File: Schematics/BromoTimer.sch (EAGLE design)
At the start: 29 parts, among them IC1 PIC16F687, IC2 7805TV, K1 G2R2A, K2 G2R2A, Q1 BC548B, Q2 BC548B, Q3 BC548B, X1 AC_IN, X4 22-23-2031, X5 AC_OUT

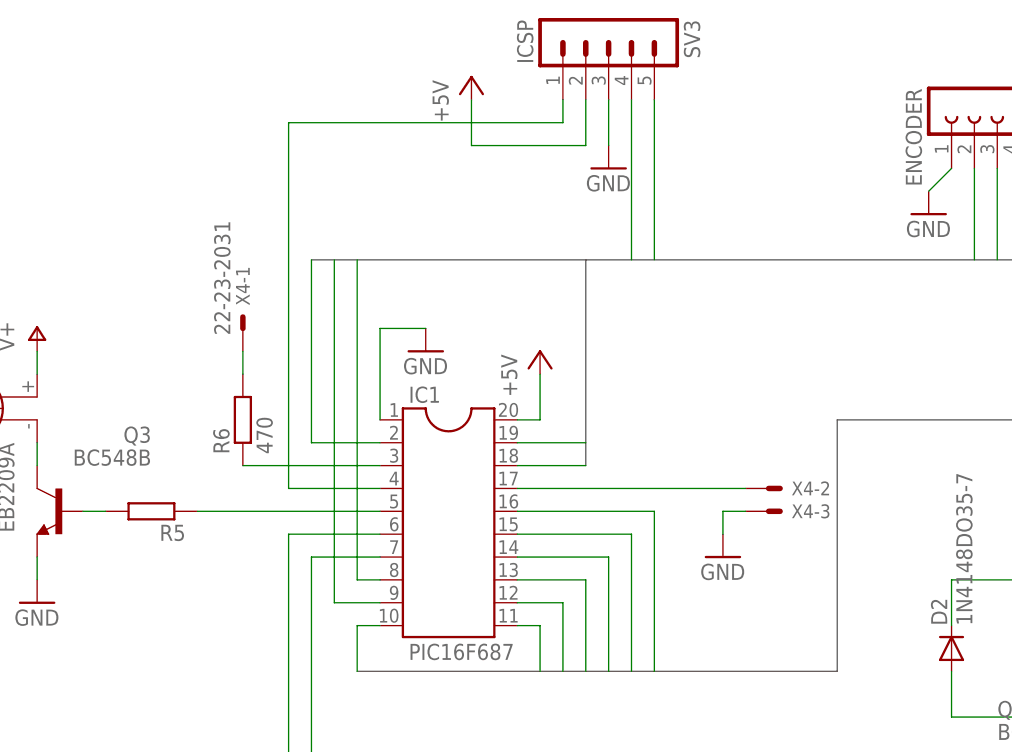
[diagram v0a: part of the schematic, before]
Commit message: Add support for lid state sensor
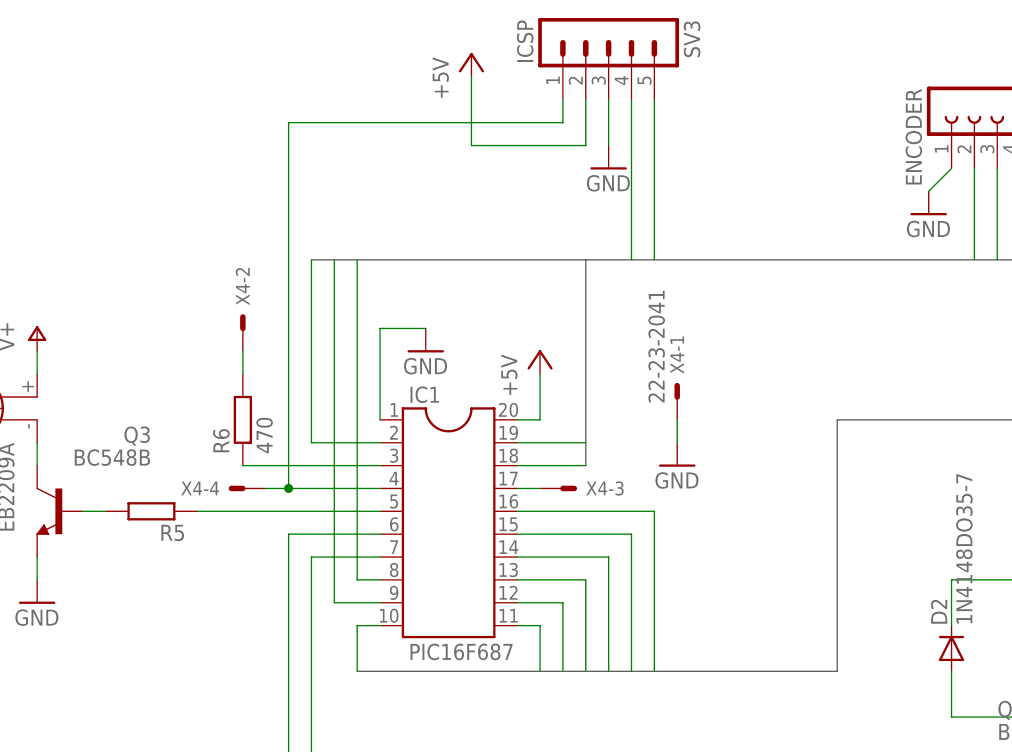
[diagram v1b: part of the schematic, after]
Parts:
- X4: value 22-23-2031 -> 22-23-2041; device con-molex:22-23-2031 -> con-molex:22-23-2041
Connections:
- net GND: now also X4-1.S; no longer X4-3.S
- net N$13: now also X4-3.S; no longer X4-2.S
- net N$15: now also X4-4.S
- net N$21: now also X4-2.S; no longer X4-1.S
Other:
- moved on the sheet: X4-1, X4-2, X4-3
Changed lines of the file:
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@@
 <?xml version="1.0" encoding="utf-8"?>
 <!DOCTYPE eagle SYSTEM "eagle.dtd">
-<eagle version="6.3">
+<eagle version="6.4">
 <drawing>
 <settings>
@@
 <part name="GND11" library="supply1" deviceset="GND" device=""/>
 <part name="P+10" library="supply1" deviceset="V+" device=""/>
-<part name="X4" library="con-molex" deviceset="22-23-2031" device=""/>
+<part name="X4" library="con-molex" deviceset="22-23-2041" device=""/>
 <part name="GND9" library="supply1" deviceset="GND" device=""/>
 <part name="SG1" library="buzzer" deviceset="EB2209A" device=""/>
@@
 <instance part="D2" gate="G$1" x="170.18" y="101.6" rot="R90"/>
 <instance part="SV3" gate="G$1" x="132.08" y="170.18" rot="R270"/>
-<instance part="P+9" gate="1" x="116.84" y="165.1"/>
+<instance part="P+9" gate="1" x="116.84" y="167.64"/>
 <instance part="GND10" gate="1" x="132.08" y="154.94"/>
 <instance part="D3" gate="1" x="40.64" y="71.12" rot="R180"/>
@@
 <instance part="GND11" gate="1" x="68.58" y="106.68"/>
 <instance part="P+10" gate="1" x="68.58" y="137.16"/>
-<instance part="X4" gate="-1" x="91.44" y="137.16" rot="R90"/>
-<instance part="X4" gate="-2" x="149.86" y="119.38"/>
-<instance part="X4" gate="-3" x="149.86" y="116.84"/>
-<instance part="GND9" gate="1" x="144.78" y="111.76"/>
+<instance part="X4" gate="-1" x="139.7" y="129.54" rot="R90"/>
+<instance part="X4" gate="-2" x="91.44" y="137.16" rot="R90"/>
+<instance part="X4" gate="-3" x="127" y="119.38"/>
+<instance part="GND9" gate="1" x="139.7" y="121.92"/>
 <instance part="SG1" gate="G$1" x="66.04" y="129.54" rot="MR270"/>
 <instance part="TR1" gate="1" x="45.72" y="25.4"/>
@@
 <instance part="X5" gate="-5" x="220.98" y="43.18"/>
 <instance part="F1" gate="1" x="27.94" y="27.94"/>
+<instance part="X4" gate="-4" x="91.44" y="119.38" rot="R180"/>
 </instances>
 <busses>
@@
 <wire x1="129.54" y1="162.56" x2="129.54" y2="157.48" width="0.1524" layer="91"/>
 <wire x1="129.54" y1="157.48" x2="116.84" y2="157.48" width="0.1524" layer="91"/>
-<wire x1="116.84" y1="157.48" x2="116.84" y2="162.56" width="0.1524" layer="91"/>
+<wire x1="116.84" y1="157.48" x2="116.84" y2="165.1" width="0.1524" layer="91"/>
 <pinref part="P+9" gate="1" pin="+5V"/>
 </segment>
@@
 </segment>
 <segment>
-<pinref part="X4" gate="-3" pin="S"/>
-<pinref part="GND9" gate="1" pin="GND"/>
-<wire x1="147.32" y1="116.84" x2="144.78" y2="116.84" width="0.1524" layer="91"/>
-<wire x1="144.78" y1="116.84" x2="144.78" y2="114.3" width="0.1524" layer="91"/>
-</segment>
-<segment>
 <pinref part="Q3" gate="G$1" pin="E"/>
 <pinref part="GND11" gate="1" pin="GND"/>
 <wire x1="68.58" y1="111.76" x2="68.58" y2="109.22" width="0.1524" layer="91"/>
+</segment>
+<segment>
+<pinref part="GND9" gate="1" pin="GND"/>
+<pinref part="X4" gate="-1" pin="S"/>
+<wire x1="139.7" y1="124.46" x2="139.7" y2="127" width="0.1524" layer="91"/>
 </segment>
 </net>
@@
 <wire x1="96.52" y1="160.02" x2="96.52" y2="119.38" width="0.1524" layer="91"/>
 <wire x1="96.52" y1="119.38" x2="106.68" y2="119.38" width="0.1524" layer="91"/>
+<pinref part="X4" gate="-4" pin="S"/>
+<wire x1="93.98" y1="119.38" x2="96.52" y2="119.38" width="0.1524" layer="91"/>
+<junction x="96.52" y="119.38"/>
 </segment>
 </net>
@@
 </segment>
 </net>
-<net name="N$13" class="0">
-<segment>
-<pinref part="IC1" gate="G$1" pin="17"/>
-<pinref part="X4" gate="-2" pin="S"/>
-<wire x1="121.92" y1="119.38" x2="147.32" y2="119.38" width="0.1524" layer="91"/>
-</segment>
-</net>
 <net name="N$18" class="0">
 <segment>
@@
 </segment>
 </net>
-<net name="N$21" class="0">
-<segment>
-<pinref part="X4" gate="-1" pin="S"/>
-<pinref part="R6" gate="G$1" pin="2"/>
-<wire x1="91.44" y1="134.62" x2="91.44" y2="132.08" width="0.1524" layer="91"/>
-</segment>
-</net>
 <net name="N$2" class="0">
 <segment>
@@
 </segment>
 </net>
+<net name="N$13" class="0">
+<segment>
+<pinref part="IC1" gate="G$1" pin="17"/>
+<pinref part="X4" gate="-3" pin="S"/>
+<wire x1="124.46" y1="119.38" x2="121.92" y2="119.38" width="0.1524" layer="91"/>
+</segment>
+</net>
+<net name="N$21" class="0">
+<segment>
+<pinref part="X4" gate="-2" pin="S"/>
+<pinref part="R6" gate="G$1" pin="2"/>
+<wire x1="91.44" y1="134.62" x2="91.44" y2="132.08" width="0.1524" layer="91"/>
+</segment>
+</net>

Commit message: Clean up R1
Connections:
- net +5V: now also R1.S; no longer R1.A
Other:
- moved on the sheet: R1
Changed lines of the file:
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@@
 <instance part="P+2" gate="1" x="124.46" y="134.62"/>
 <instance part="GND3" gate="1" x="193.04" y="142.24"/>
-<instance part="GND4" gate="1" x="228.6" y="139.7"/>
+<instance part="GND4" gate="1" x="223.52" y="149.86"/>
 <instance part="P+3" gate="1" x="198.12" y="170.18"/>
-<instance part="R1" gate="G$1" x="220.98" y="147.32"/>
+<instance part="R1" gate="G$1" x="220.98" y="137.16"/>
 <instance part="R2" gate="G$1" x="200.66" y="147.32" rot="R180"/>
-<instance part="P+4" gate="1" x="215.9" y="142.24"/>
+<instance part="P+4" gate="1" x="228.6" y="144.78"/>
 <instance part="Q1" gate="G$1" x="185.42" y="86.36"/>
 <instance part="Q2" gate="G$1" x="185.42" y="43.18"/>
@@
 </segment>
 <segment>
-<pinref part="P+4" gate="1" pin="+5V"/>
-<wire x1="215.9" y1="139.7" x2="215.9" y2="137.16" width="0.1524" layer="91"/>
-<pinref part="R1" gate="G$1" pin="A"/>
-<wire x1="215.9" y1="137.16" x2="220.98" y2="137.16" width="0.1524" layer="91"/>
-<wire x1="220.98" y1="137.16" x2="220.98" y2="142.24" width="0.1524" layer="91"/>
-</segment>
-<segment>
 <pinref part="SV3" gate="G$1" pin="2"/>
 <wire x1="129.54" y1="162.56" x2="129.54" y2="157.48" width="0.1524" layer="91"/>
@@
 <junction x="187.96" y="109.22"/>
 </segment>
+<segment>
+<pinref part="P+4" gate="1" pin="+5V"/>
+<wire x1="228.6" y1="142.24" x2="228.6" y2="137.16" width="0.1524" layer="91"/>
+<pinref part="R1" gate="G$1" pin="S"/>
+<wire x1="228.6" y1="137.16" x2="226.06" y2="137.16" width="0.1524" layer="91"/>
+</segment>
 </net>
 <net name="GND" class="0">
@@
 <pinref part="GND4" gate="1" pin="GND"/>
 <pinref part="SV2" gate="G$1" pin="12"/>
-<wire x1="228.6" y1="142.24" x2="228.6" y2="152.4" width="0.1524" layer="91"/>
-<wire x1="228.6" y1="152.4" x2="223.52" y2="152.4" width="0.1524" layer="91"/>
 <wire x1="223.52" y1="152.4" x2="223.52" y2="154.94" width="0.1524" layer="91"/>
 </segment>
@@
 <segment>
 <pinref part="SV2" gate="G$1" pin="11"/>
-<wire x1="220.98" y1="154.94" x2="220.98" y2="152.4" width="0.1524" layer="91"/>
+<wire x1="220.98" y1="154.94" x2="220.98" y2="142.24" width="0.1524" layer="91"/>
 <pinref part="R1" gate="G$1" pin="E"/>
 </segment>

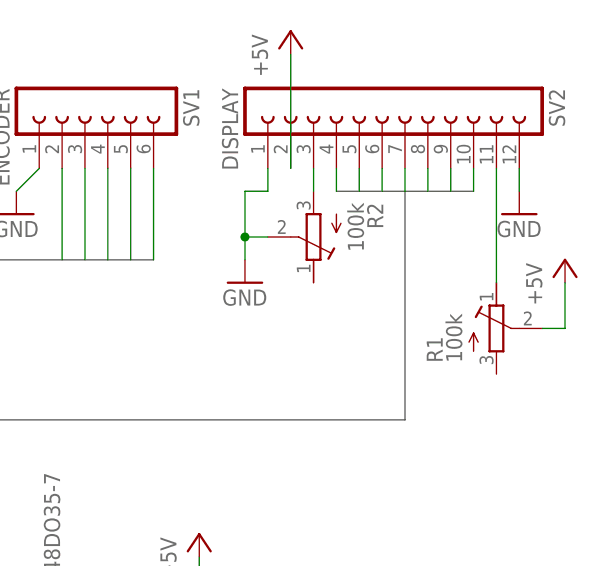
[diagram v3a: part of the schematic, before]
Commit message: Correct trimmer footprints
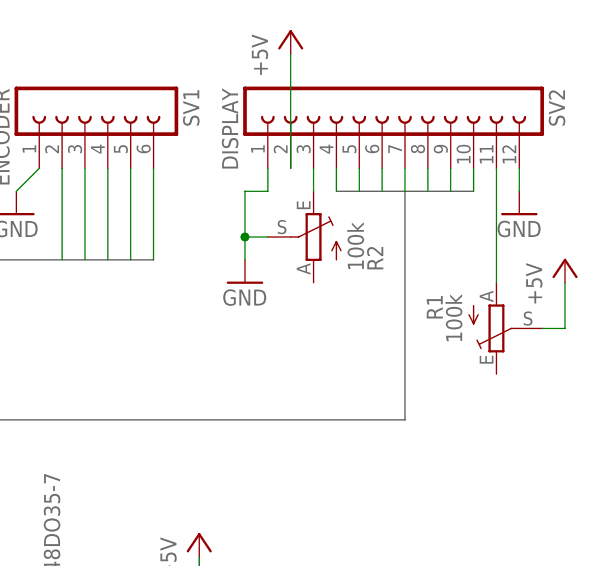
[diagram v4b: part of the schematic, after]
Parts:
- R1, R2: device rcl:R-TRIMMT93YB -> pot:TRIM_EU-CA14H
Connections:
- net N$1: now also R1.A; no longer R1.E
- net N$3: now also R2.E; no longer R2.A
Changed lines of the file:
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@@
 <part name="GND4" library="supply1" deviceset="GND" device=""/>
 <part name="P+3" library="supply1" deviceset="+5V" device=""/>
-<part name="R1" library="rcl" deviceset="R-TRIMM" device="T93YB" value="100k"/>
-<part name="R2" library="rcl" deviceset="R-TRIMM" device="T93YB" value="100k"/>
+<part name="R1" library="pot" deviceset="TRIM_EU-" device="CA14H" value="100k"/>
+<part name="R2" library="pot" deviceset="TRIM_EU-" device="CA14H" value="100k"/>
 <part name="P+4" library="supply1" deviceset="+5V" device=""/>
 <part name="Q1" library="transistor-npn" deviceset="BC548*" device="" technology="B" value="BC548B"/>
@@
 <instance part="GND4" gate="1" x="223.52" y="149.86"/>
 <instance part="P+3" gate="1" x="198.12" y="170.18"/>
-<instance part="R1" gate="G$1" x="220.98" y="137.16"/>
-<instance part="R2" gate="G$1" x="200.66" y="147.32" rot="R180"/>
+<instance part="R1" gate="1" x="220.98" y="137.16" rot="MR180"/>
+<instance part="R2" gate="1" x="200.66" y="147.32" rot="MR0"/>
 <instance part="P+4" gate="1" x="228.6" y="144.78"/>
 <instance part="Q1" gate="G$1" x="185.42" y="86.36"/>
@@
 <pinref part="P+4" gate="1" pin="+5V"/>
 <wire x1="228.6" y1="142.24" x2="228.6" y2="137.16" width="0.1524" layer="91"/>
-<pinref part="R1" gate="G$1" pin="S"/>
+<pinref part="R1" gate="1" pin="S"/>
 <wire x1="228.6" y1="137.16" x2="226.06" y2="137.16" width="0.1524" layer="91"/>
 </segment>
@@
 <wire x1="195.58" y1="152.4" x2="193.04" y2="152.4" width="0.1524" layer="91"/>
 <wire x1="193.04" y1="152.4" x2="193.04" y2="147.32" width="0.1524" layer="91"/>
-<pinref part="R2" gate="G$1" pin="S"/>
+<pinref part="R2" gate="1" pin="S"/>
 <wire x1="193.04" y1="147.32" x2="193.04" y2="144.78" width="0.1524" layer="91"/>
 <wire x1="195.58" y1="147.32" x2="193.04" y2="147.32" width="0.1524" layer="91"/>
@@
 <wire x1="106.68" y1="104.14" x2="104.14" y2="104.14" width="0.1524" layer="91"/>
 <wire x1="104.14" y1="104.14" x2="104.14" y2="99.06" width="0.1524" layer="91"/>
-</segment>
-</net>
-<net name="N$1" class="0">
-<segment>
-<pinref part="SV2" gate="G$1" pin="11"/>
-<wire x1="220.98" y1="154.94" x2="220.98" y2="142.24" width="0.1524" layer="91"/>
-<pinref part="R1" gate="G$1" pin="E"/>
-</segment>
-</net>
-<net name="N$3" class="0">
-<segment>
-<pinref part="SV2" gate="G$1" pin="3"/>
-<pinref part="R2" gate="G$1" pin="A"/>
-<wire x1="200.66" y1="154.94" x2="200.66" y2="152.4" width="0.1524" layer="91"/>
 </segment>
 </net>
@@
 </segment>
 </net>
+<net name="N$3" class="0">
+<segment>
+<pinref part="SV2" gate="G$1" pin="3"/>
+<pinref part="R2" gate="1" pin="E"/>
+<wire x1="200.66" y1="154.94" x2="200.66" y2="152.4" width="0.1524" layer="91"/>
+</segment>
+</net>
+<net name="N$1" class="0">
+<segment>
+<pinref part="SV2" gate="G$1" pin="11"/>
+<pinref part="R1" gate="1" pin="A"/>
+<wire x1="220.98" y1="154.94" x2="220.98" y2="142.24" width="0.1524" layer="91"/>
+</segment>
+</net>

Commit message: Increase default keepout
Default keepout increased to 25mil. Also, inverted function of RC6 and RC7.
Change is also made in code to reflect this.
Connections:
- net L1: now also IC1.9; no longer IC1.8
- net L2: now also IC1.8; no longer IC1.9
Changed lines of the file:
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@@
 <classes>
 <class number="0" name="default" width="0.4064" drill="0">
-<clearance class="0" value="0.4064"/>
+<clearance class="0" value="0.635"/>
 </class>
 <class number="1" name="HV" width="1.27" drill="0">
@@
 </segment>
 <segment>
-<pinref part="IC1" gate="G$1" pin="8"/>
-<wire x1="106.68" y1="109.22" x2="104.14" y2="109.22" width="0.1524" layer="91"/>
-<wire x1="104.14" y1="109.22" x2="104.14" y2="144.78" width="0.1524" layer="91"/>
-</segment>
-</net>
-<net name="L2" class="0">
-<segment>
-<pinref part="SV1" gate="G$1" pin="3"/>
-<wire x1="175.26" y1="154.94" x2="175.26" y2="144.78" width="0.1524" layer="91"/>
-</segment>
-<segment>
 <pinref part="IC1" gate="G$1" pin="9"/>
 <wire x1="106.68" y1="106.68" x2="101.6" y2="106.68" width="0.1524" layer="91"/>
@@
 </segment>
 </net>
+<net name="L2" class="0">
+<segment>
+<pinref part="SV1" gate="G$1" pin="3"/>
+<wire x1="175.26" y1="154.94" x2="175.26" y2="144.78" width="0.1524" layer="91"/>
+</segment>
+<segment>
+<wire x1="104.14" y1="109.22" x2="104.14" y2="144.78" width="0.1524" layer="91"/>
+<pinref part="IC1" gate="G$1" pin="8"/>
+<wire x1="104.14" y1="109.22" x2="106.68" y2="109.22" width="0.1524" layer="91"/>
+</segment>
+</net>
